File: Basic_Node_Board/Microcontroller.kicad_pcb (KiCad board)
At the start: 4 copper layers, 100 x 100 mm, 31 parts, among them J1 Conn_01x02, J4 Conn_01x02_Pin, U2 ESP32-DEVKIT-C, U3 TPS54560BQDDARQ1, U6 TJA1050T/CM,118

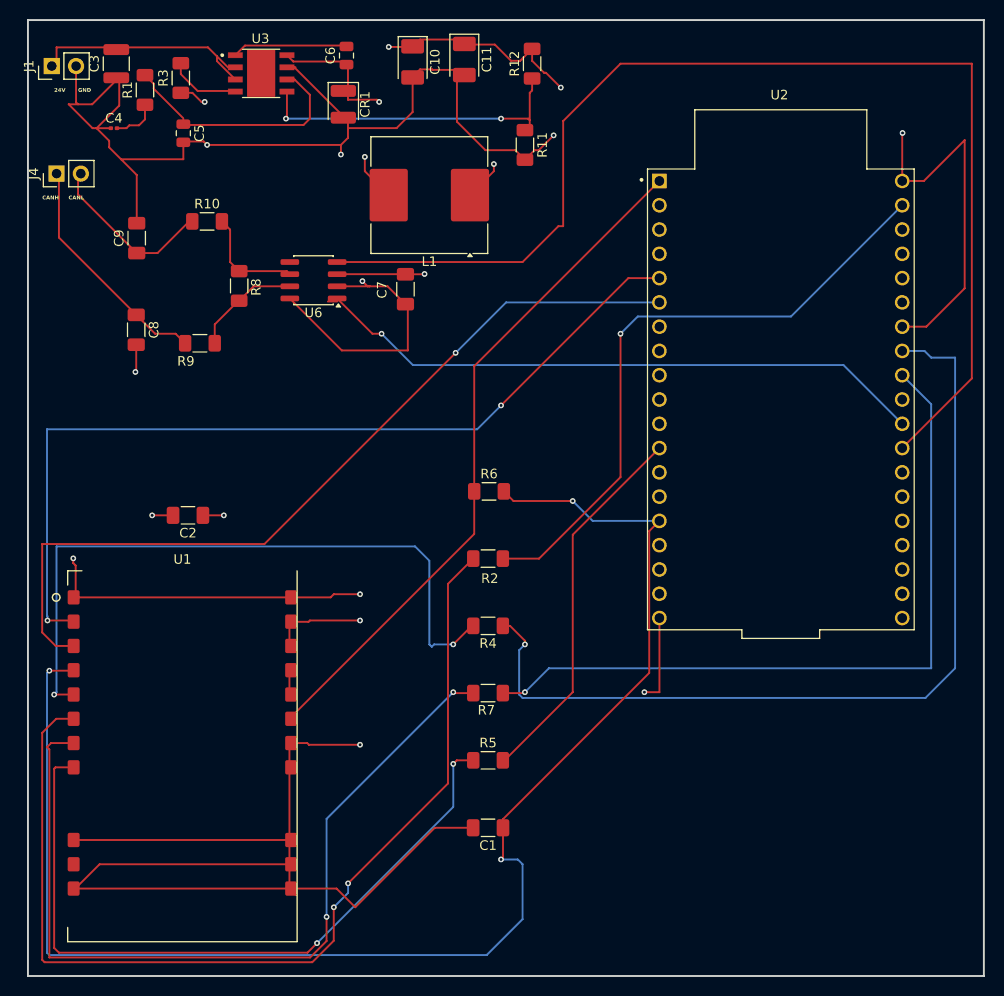
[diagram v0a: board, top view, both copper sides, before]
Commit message: updated telem pcb, will do mcu next on this branch. Key actions: corrected ground plane to make it a plane, not a few wires, which is important for heat disipation. I made the Vcc plane another ground plane instead, since it wasnt really necessary for Vcc, and a second gnd plane should better help with heat. I also did not extend the ground plane under the ebyte, since their instructions say to avoid routing power underneath. Its a bit confusing, since there appear to be some pads under the module for gnd that we arent using. ive heard that having a gnd plane under rf module can create problematic couping, so would rather be safe and do this, should still be plenty able to dissipate heat without it. the inductor and diode for the buck converter were both too small. The inductor had double the ESR of the suggested TI on, so likely wouldnt be great. The diode would never survive the buck converter. The diode i am using is the one TI suggested from the web-bench, and is considerabley larger, and rated for 5 Amps. This is important for a 2A buck. The diode often temporarily has to more than the bucks output. Also updated the CAN Controller (the TJA...) I think the circuit that was being used there was intended as a test circuit, not an implementation. we would never want to add extra capacitacne on CANH and CANL, i think those capacitors were for testing the modules ability to drive a network. The new CAN circuit is now just an optional termination resistor, and a local capacitor between gnd and Vcc. I removed partslib, and other parts that were added here. all parts (symbols, footprints, 3D stuff) should go in the seperate partslib repo. I suggest cloning partslib adjascent to your pcb directory, and then setting up your kicad paths appropriately (will write a memo on this later)
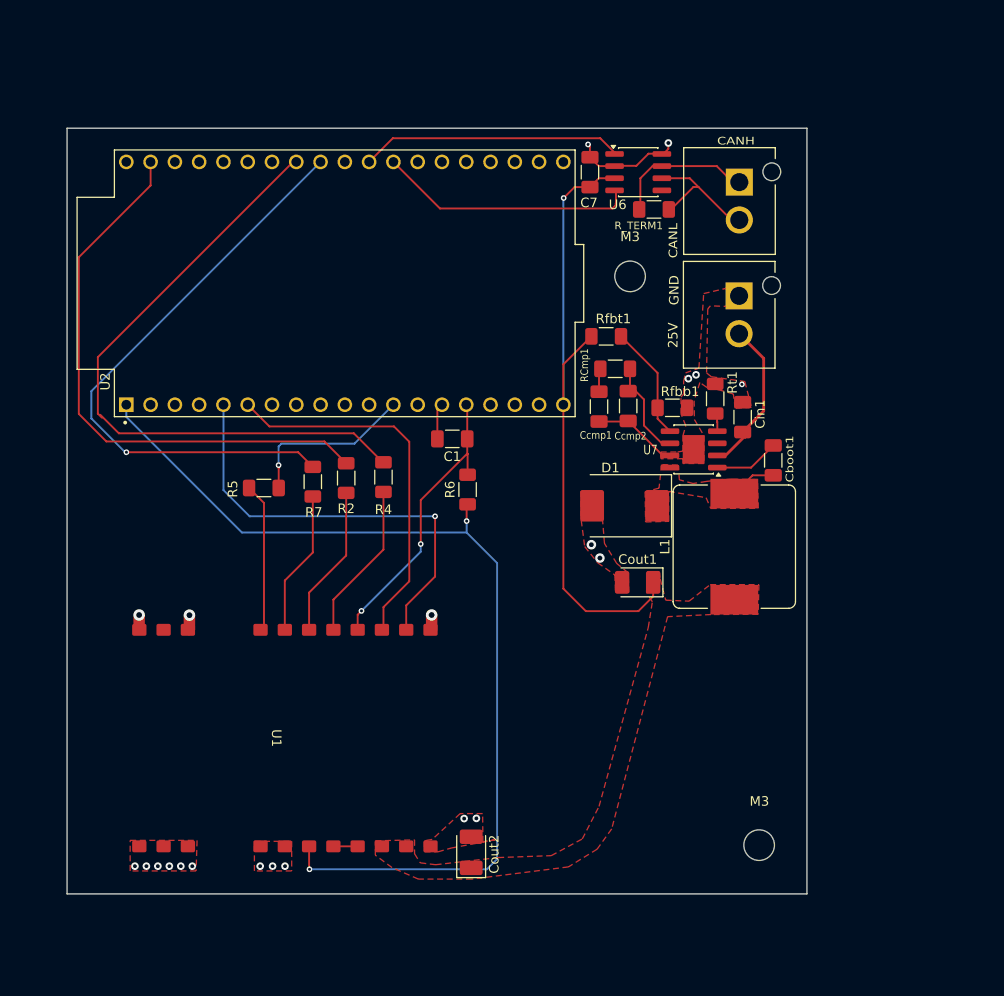
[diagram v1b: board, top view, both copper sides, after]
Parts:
- removed C10, C11: 47uF, Capacitor_Tantalum_SMD:CP_EIA-3528-21_Kemet-B_HandSolder
- removed C2: 100uF, Capacitor_SMD:C_1206_3216Metric_Pad1.33x1.80mm_HandSolder
- removed C3: 30uF, Capacitor_SMD:C_1210_3225Metric
- removed C4: 82nF, Capacitor_SMD:C_0201_0603Metric
- removed C5: 100pF, Capacitor_SMD:C_0805_2012Metric
- removed C6: 100nF, Capacitor_SMD:C_0805_2012Metric
- removed C8, C9: 30p, Capacitor_SMD:C_1206_3216Metric_Pad1.33x1.80mm_HandSolder
- removed CR1: SS34, Diode_SMD:D_1210_3225Metric
- removed R1: 5.1k, Resistor_SMD:R_1206_3216Metric_Pad1.30x1.75mm_HandSolder
- removed R10, R9: 0, Resistor_SMD:R_1206_3216Metric_Pad1.30x1.75mm_HandSolder
- removed R11: 10k, Resistor_SMD:R_1206_3216Metric_Pad1.30x1.75mm_HandSolder
- removed R12: 56.2k, Resistor_SMD:R_1206_3216Metric_Pad1.30x1.75mm_HandSolder
- removed R3: 243k, Resistor_SMD:R_1206_3216Metric_Pad1.30x1.75mm_HandSolder
- removed R8: 120, Resistor_SMD:R_1206_3216Metric_Pad1.30x1.75mm_HandSolder
- removed U3: TPS54560BQDDARQ1, PROVE-footprints:VREG_LM5017MR_NOPB
- added Cboot1: 100nF, Capacitor_SMD:C_1206_3216Metric_Pad1.33x1.80mm_HandSolder, F.Cu at (113.5, 70.8)
- added Ccmp1: 10nF, Capacitor_SMD:C_1206_3216Metric_Pad1.33x1.80mm_HandSolder, F.Cu at (95.2, 65.1)
- added Ccmp2: 10pF, Capacitor_SMD:C_1206_3216Metric_Pad1.33x1.80mm_HandSolder, F.Cu at (98.3, 65.1)
- added Cin1: 4.7uF, Capacitor_SMD:C_1206_3216Metric_Pad1.33x1.80mm_HandSolder, F.Cu at (110.3, 66.2)
- added Cout1: 47uF, Capacitor_Tantalum_SMD:CP_EIA-3528-21_Kemet-B_HandSolder, F.Cu at (99.3, 83.5)
- added Cout2: 47uF, Capacitor_Tantalum_SMD:CP_EIA-3528-21_Kemet-B_HandSolder, F.Cu at (81.9, 111.8)
- added D1: B560CQ-13-F, Diode_SMD:D_SMC, F.Cu at (97.9, 75.5)
- added M3: MountingHole, MountingHole:MountingHole_3.2mm_M3, F.Cu at (98.5, 51.5)
- added M3_1: MountingHole, MountingHole:MountingHole_3.2mm_M3, F.Cu at (112.0, 111.0)
- added RCmp1: 18.2kOhm, Resistor_SMD:R_1206_3216Metric_Pad1.30x1.75mm_HandSolder, F.Cu at (96.9, 61.2)
- added R_TERM1: 120, Resistor_SMD:R_1206_3216Metric_Pad1.30x1.75mm_HandSolder, F.Cu at (101.0, 44.5)
- added Rfbb1: 11kOhm, Resistor_SMD:R_1206_3216Metric_Pad1.30x1.75mm_HandSolder, F.Cu at (102.9, 65.2)
- added Rfbt1: 61.9kOhm, Resistor_SMD:R_1206_3216Metric_Pad1.30x1.75mm_HandSolder, F.Cu at (96.0, 57.8)
- added Rt1: 147kOhm, Resistor_SMD:R_1206_3216Metric_Pad1.30x1.75mm_HandSolder, F.Cu at (107.4, 64.3)
- added U7: TPS54560BQDDARQ1, Package_SO:SOIC-8-1EP_3.9x4.9mm_P1.27mm_EP2.29x3mm, F.Cu at (105.1, 69.6)
- J1, J4: footprint Connector_PinHeader_2.54mm:PinHeader_1x02_P2.54mm_Vertical -> PROVE-footprints:TE_1877285-2
- L1: value 47uH -> 22uH; footprint Inductor_SMD:L_Coilcraft_MSS1260T-XXX -> Inductor_SMD:L_Bourns_SRP1245A
- U1: footprint PROVE-footprints:E22P-915M30S_revised -> PROVE-footprints:E22P-915M30S
- moved J1 75.5 mm to (108.9, 55.5), turned to -90 degrees
- moved J4 70.5 mm to (108.9, 43.6), turned to -90 degrees
- moved L1 48.7 mm to (109.4, 79.8), turned to 90 degrees
- moved U2 47.2 mm to (68.7, 52.2), turned to 90 degrees
- moved C1 40.9 mm to (79.9, 68.5)
- moved R5 36.9 mm to (60.2, 73.6)
- moved U6 35.8 mm to (99.3, 40.6), turned to 0 degrees
- moved R7 28.7 mm to (65.3, 73.0), turned to -90 degrees
- moved C7 22.9 mm to (94.3, 40.6), turned to -90 degrees
- moved R4 19.0 mm to (72.7, 72.5), turned to -90 degrees
- moved R2 17.1 mm to (68.8, 72.6), turned to -90 degrees
- moved U1 9.53 mm to (61.0, 99.8), turned to -90 degrees
- moved R6 2.25 mm to (81.5, 73.8), turned to 90 degrees
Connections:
- C1 pad 2: GND -> Net-(U2-GND1)
- J1 pad 1: /24V -> GND
- J1 pad 2: GND -> /25_To_5p3V_step_down/25V_In
- U2 pad 10: Net-(J2-Pin_10) -> unconnected-(U2-IO26-Pad10)
- U2 pad 11: Net-(J2-Pin_11) -> unconnected-(U2-IO27-Pad11)
- U2 pad 13: Net-(J2-Pin_13) -> unconnected-(U2-IO12-Pad13)
- U2 pad 14: Net-(J2-Pin_14) -> Net-(U2-GND1)
- U2 pad 16: Net-(J2-Pin_16) -> unconnected-(U2-SD2-Pad16)
- U2 pad 17: Net-(J2-Pin_17) -> unconnected-(U2-SD3-Pad17)
- U2 pad 18: Net-(J2-Pin_18) -> unconnected-(U2-CMD-Pad18)
- U2 pad 2: Net-(J2-Pin_2) -> unconnected-(U2-EN-Pad2)
- U2 pad 20: Net-(J3-Pin_19) -> unconnected-(U2-CLK-Pad20)
- U2 pad 21: Net-(J3-Pin_18) -> unconnected-(U2-SD0-Pad21)
- U2 pad 22: Net-(J3-Pin_17) -> unconnected-(U2-SD1-Pad22)
- U2 pad 23: Net-(J3-Pin_16) -> unconnected-(U2-IO15-Pad23)
- U2 pad 24: Net-(J3-Pin_15) -> unconnected-(U2-IO2-Pad24)
- U2 pad 25: Net-(J3-Pin_14) -> unconnected-(U2-IO0-Pad25)
- U2 pad 26: Net-(J3-Pin_13) -> unconnected-(U2-IO4-Pad26)
- U2 pad 29: Net-(J3-Pin_10) -> unconnected-(U2-IO5-Pad29)
- U2 pad 3: Net-(J2-Pin_3) -> unconnected-(U2-SENSOR_VP-Pad3)
- U2 pad 33: Net-(J3-Pin_6) -> unconnected-(U2-IO21-Pad33)
- U2 pad 34: Net-(J3-Pin_5) -> unconnected-(U2-RXD0-Pad34)
- U2 pad 35: Net-(J3-Pin_4) -> unconnected-(U2-TXD0-Pad35)
- U2 pad 36: Net-(J3-Pin_3) -> unconnected-(U2-IO22-Pad36)
- U2 pad 38: GND -> unconnected-(U2-GND3-Pad38)
- U2 pad 4: Net-(J2-Pin_4) -> unconnected-(U2-SENSOR_VN-Pad4)
- U2 pad 7: Net-(J2-Pin_7) -> unconnected-(U2-IO32-Pad7)
- U2 pad 8: Net-(J2-Pin_8) -> unconnected-(U2-IO33-Pad8)
- U2 pad 9: Net-(J2-Pin_9) -> unconnected-(U2-IO25-Pad9)
- U6 pad 6: Net-(U6-CANL) -> /CANL
- U6 pad 7: Net-(U6-CANH) -> /CANH
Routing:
- net GND: track 497.3 -> 27.6 mm, vias 11 -> 21
- net 5.3V OUT: track 203.6 -> 68.1 mm, vias 7 -> 1
- net Net-(U1-NRST): track 152.2 -> 31.0 mm, vias 3 -> 2
- net Net-(U2-IO16): track 124.7 -> 27.0 mm
- net Net-(U1-MOSI): track 105.2 -> 15.9 mm, vias 2 -> 0
- net Net-(U1-SCK): track 88.9 -> 15.2 mm, vias 2 -> 0
- net Net-(U1-NSS): track 76.5 -> 15.6 mm, vias 2 -> 0
- net Net-(U1-MISO): track 71.9 -> 16.6 mm, vias 2 -> 0
- net Net-(U1-BUSY): track 88.3 -> 39.4 mm, vias 1 -> 0
- net Net-(U1-DIO1): track 93.6 -> 45.8 mm, vias 2 -> 1
- net Net-(U2-IO17): track 65.5 -> 27.5 mm, vias 1 -> 0
- net Net-(U3-FB): track 34.2 -> 0.00 mm, vias 2 -> 0
- net Net-(U1-EN): track 72.6 -> 102.8 mm, vias 0 -> 2
- net Net-(U2-IO19): track 94.2 -> 67.4 mm, vias 1 -> 0
- net Net-(U3-COMP): track 25.8 -> 0.00 mm
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- added copper zone on F.Cu, net 5.3V OUT
- added copper zone on F.Cu, net GND
- added copper zone on In1.Cu, net GND
- added copper zone on In2.Cu, net GND
- added copper zone on F.Cu, net Net-(U7-SW)
- removed copper zone on In1.Cu, net 5.3V OUT
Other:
- board size 100 x 100 mm -> 77.4 x 80.1 mm
- board text added: "25V"
- board text added: "M3"
- board text removed: "24V"
